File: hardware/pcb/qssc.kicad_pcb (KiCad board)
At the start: 6 copper layers, 210 x 140 mm, 126 parts, among them J1 FT232RL, J10 USB-C, J12 BTB_HOST, J2 5V Barrel, J3 SMA, J4 12V LED, J7 RESET, J8 MW_GATE, J9 JTAG, U1 XC7A35T-1CSG324C, U3 ADF4351BCPZ, U5 GVA-84+, U8 W25Q128JVSIQ, Y1 100MHz TCXO

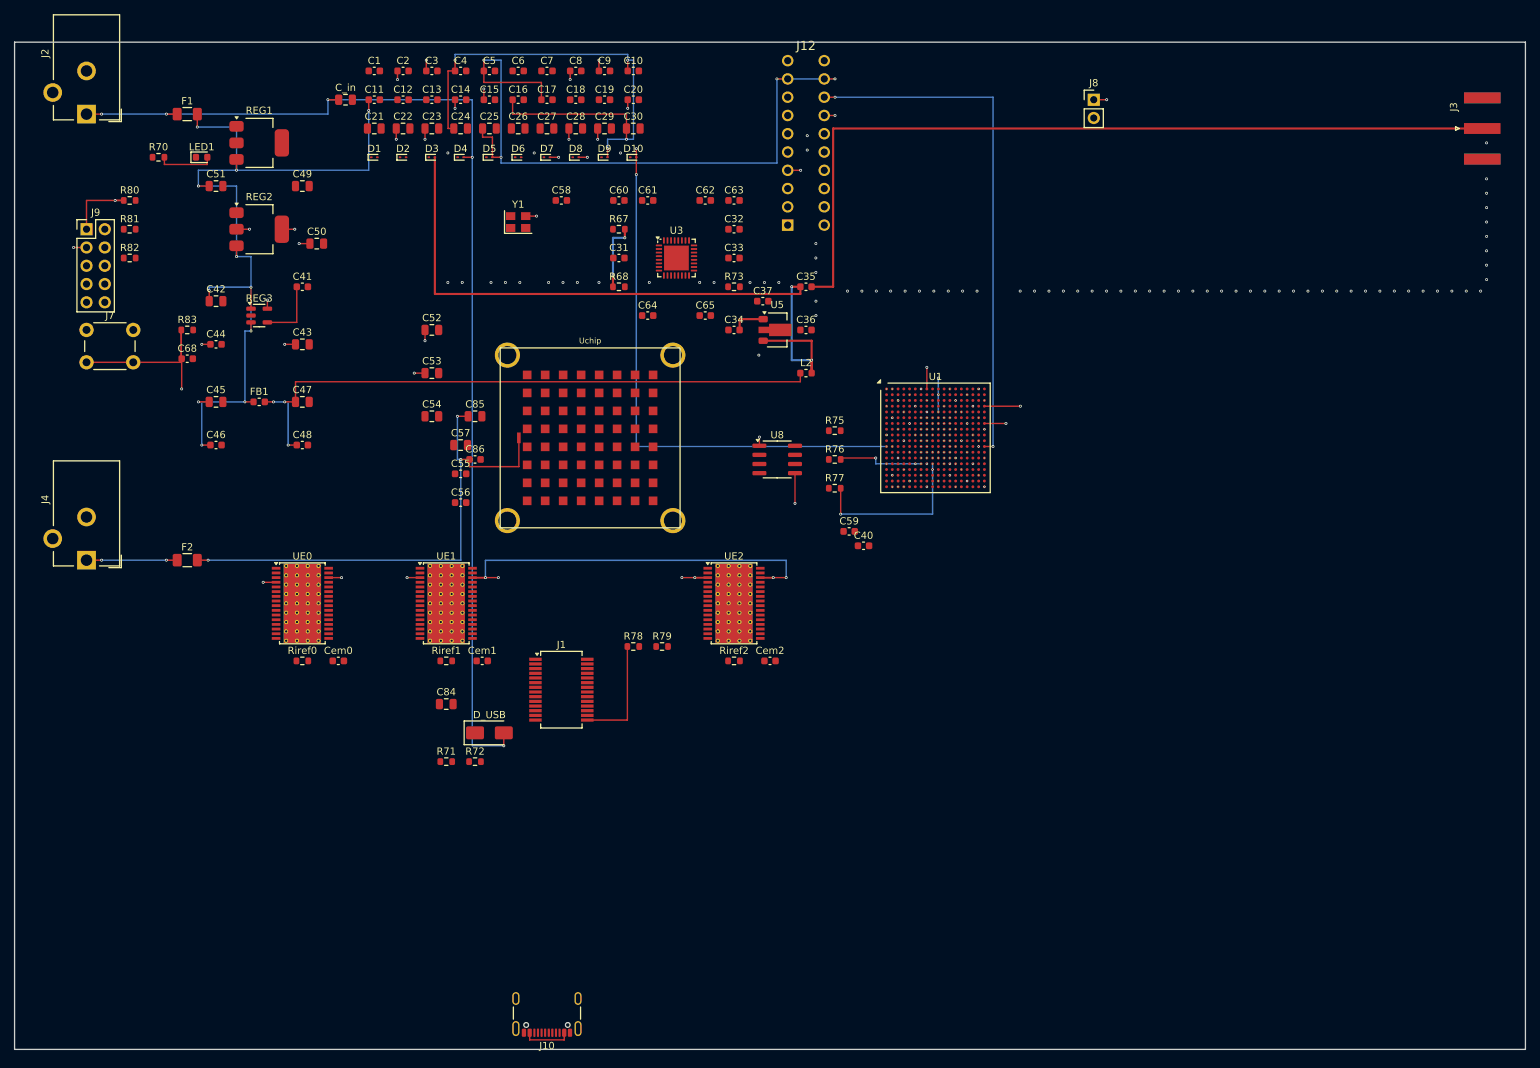
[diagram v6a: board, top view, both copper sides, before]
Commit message: route: 2.5mm dog-bone chip fanout (128 die vias) + planes poured, DRC 0/0/0
_chip_fanout was a no-op deferring all 128 die nets to FreeRouting, which
plateaued (~474 unrouted). Restore a real dog-bone fanout for the 2.5 mm 8x8
die grid: 0.15 mm stub on the pad's own layer + 0.20 mm through-via 1.0 mm out
(in the 1.3 mm inter-pad gap), escaped on the opposite clear surface by the
line router. At 2.5 mm pitch the via clears adjacent pads by 0.80 mm -- the
68/98 shorting_items of the old 0.30 mm design cannot occur. The fixed 3 mm
escape that shorted adjacent-row escapes on the same column is GONE; the line
router routes via->target on the clear layer (marking keepout, no overlaps).

EM_ANODE (+12V_EMIT) is left to the power router. Planes poured on both boards
(GND + +3V3 zones). Both boards DRC 0 violations / 0 unconnected / 0 shorts.

Via->target closure for the 64 emitter_cat (main) + 64 DET_IN (head) + 64
DET_TIA (head) is still pending -- the line router cannot place 64 long
single-layer crossings; FreeRouting closes the reduced problem next.

Co-Authored-By: Claude Code <noreply@anthropic.com>
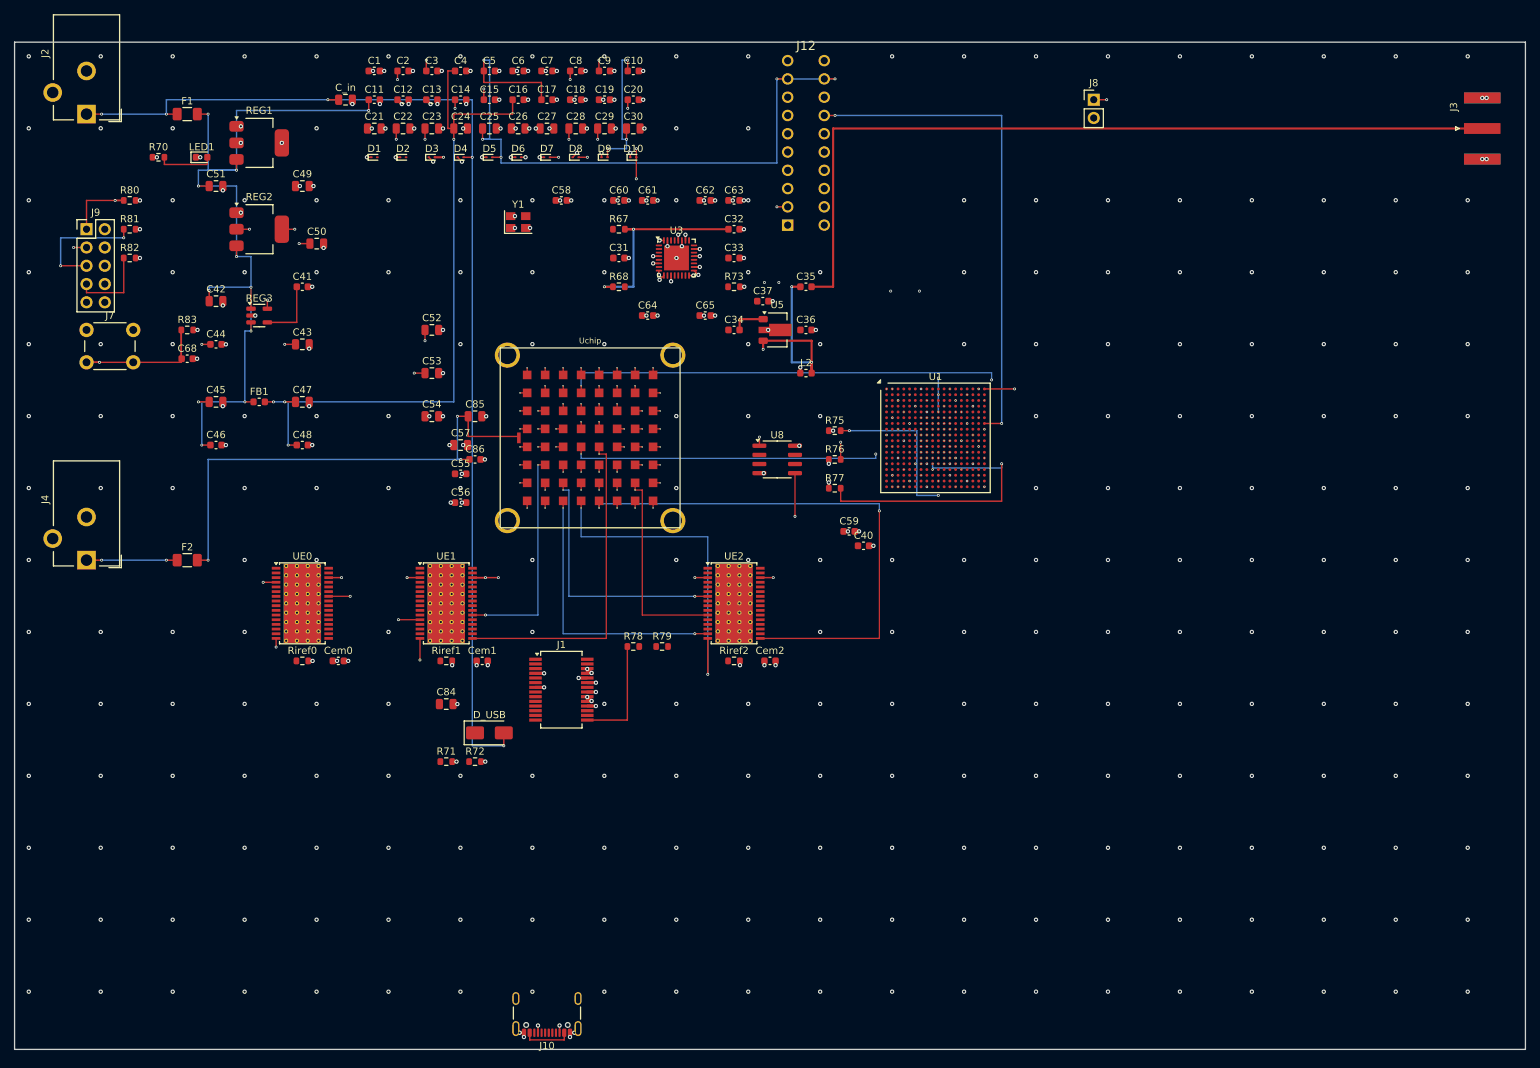
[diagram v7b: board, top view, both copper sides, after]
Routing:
- net emitter_cat11: track 0.00 -> 198.6 mm, vias 0 -> 3
- net emitter_cat35: track 0.00 -> 147.7 mm, vias 0 -> 3
- net clk_100mhz: track 80.6 -> 0.00 mm, vias 2 -> 0
- net emitter_cat60: track 0.00 -> 75.8 mm, vias 0 -> 2
- net GND: track 0.00 -> 75.2 mm, vias 129 -> 414
- net adc_cs3: track 73.2 -> 0.00 mm, vias 2 -> 0
- net adc_miso: track 70.1 -> 0.00 mm, vias 2 -> 0
- net emitter_cat21: track 0.00 -> 67.9 mm, vias 0 -> 2
- net emitter_cat31: track 0.00 -> 66.9 mm, vias 0 -> 2
- net adc_convst: track 0.00 -> 64.0 mm, vias 0 -> 3
- net +5V_RF: track 163.7 -> 116.7 mm, vias 7 -> 8
- net emitter_cat59: track 0.00 -> 46.7 mm, vias 0 -> 2
- net emitter_cat36: track 0.00 -> 46.2 mm, vias 0 -> 1
- net emitter_cat58: track 0.00 -> 38.6 mm, vias 0 -> 2
- net emitter_cat50: track 0.00 -> 35.9 mm, vias 0 -> 2
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- added copper zone on In2.Cu, net +3V3
- added copper zone on In1.Cu, net GND

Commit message: fpga: JTAG J9 pin 9 GND->+3V3 (VREF) per Xilinx 10-pin pinout
The JTAG header J9 (2x5 2.54mm) matched the Xilinx 10-pin JTAG form on
TCK/TDO/TMS/TDI (pins 1/3/5/7) and GND (even), but pin 9 was GND instead
of VREF.  Without VREF only FTDI-generic JTAG cables worked; the Digilent
JTAG-HS3 and Xilinx Platform Cable II need pin 9 = VREF to power their IO
buffers.  JTAG balls sit in bank 0 (VCCO_0 = +3V3), so VREF = +3V3.

Also verified (no change needed) the CSG324 land pattern vs UG475: the
official KiCad Package_BGA:Xilinx_CSG324 footprint is 324 balls / 18x18 /
0.8 mm pitch / 15x15 mm body, copper L=0.40 mm, NSMD via footprint-level
solder_mask_margin 0.05 => mask opening M=0.50 mm = UG475 M.  Documented
in DATASHEETS.md.  Applied to the main board on disk surgically (the head
board is mid-autoroute and left untouched).

Co-Authored-By: Claude Code <noreply@anthropic.com>
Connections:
- J9 pad 9: GND -> +3V3
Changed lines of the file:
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@@
 			(layers "*.Cu" "*.Mask")
 			(remove_unused_layers no)
-			(net 18 "GND")
+			(net 5 "+3V3")
 		)
 		(pad "10" thru_hole oval
